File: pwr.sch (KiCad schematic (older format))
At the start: 54 parts, among them U1 FT601, U10 MIC94310, U11 PAM2305, U4 ECP5, U6 PAM2305, U7 NCP186, U8 MIC94310, U9 MIC94310, X2 CONN_01X08

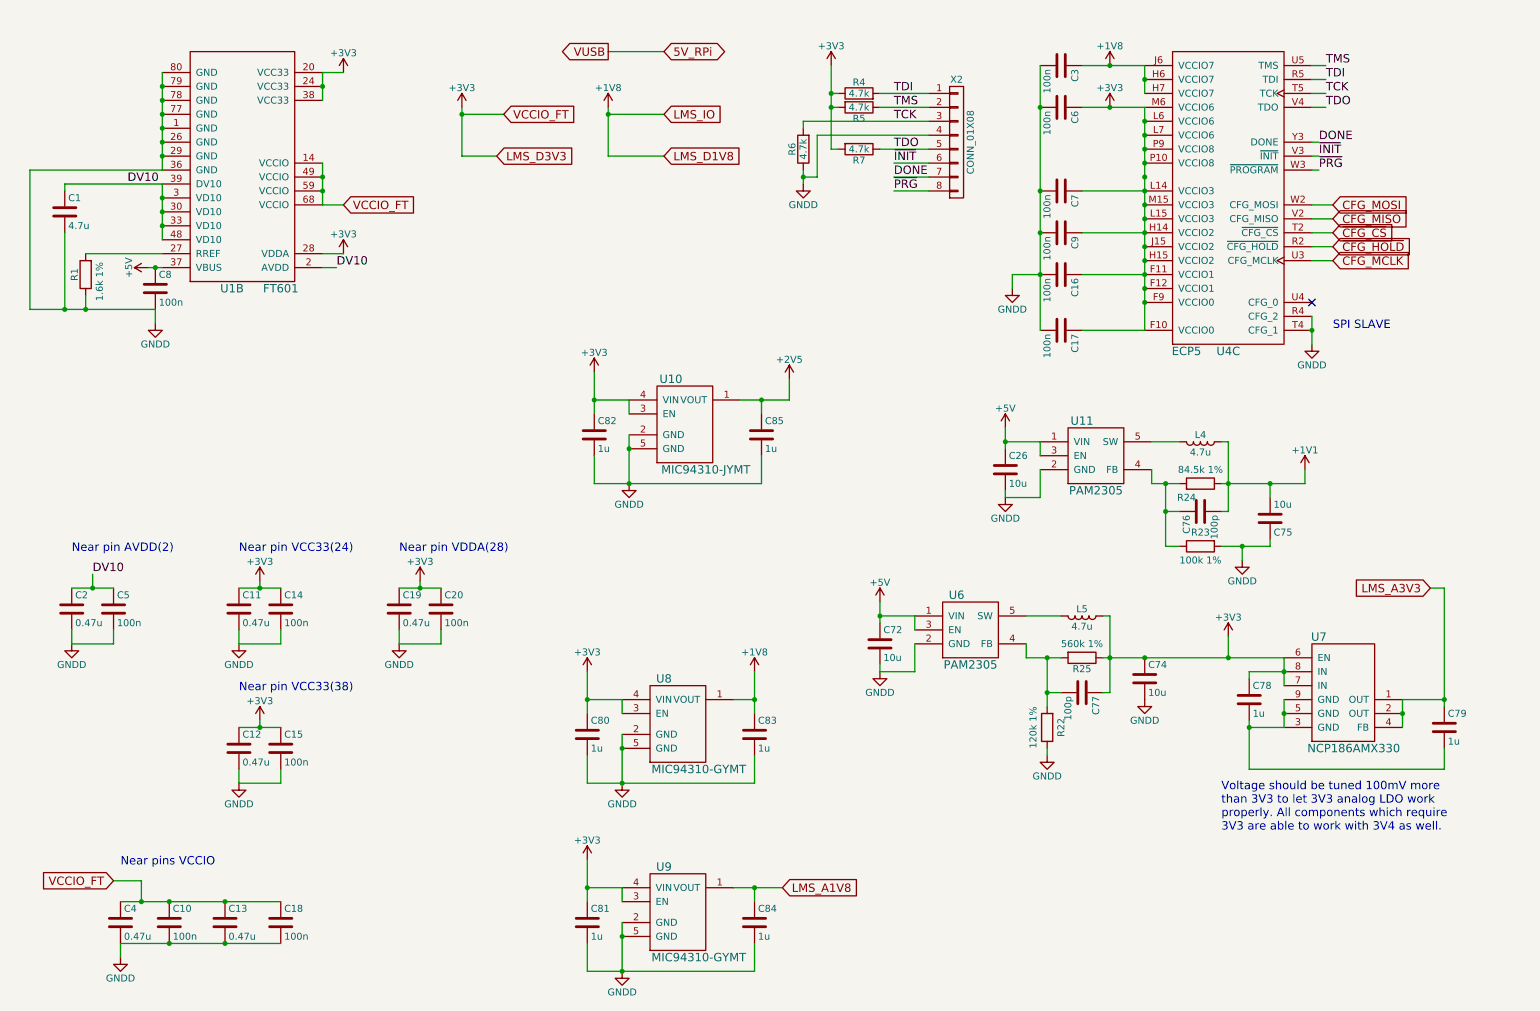
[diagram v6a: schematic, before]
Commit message: Start placing RF. Shield is ready. Fixed some net bugs.
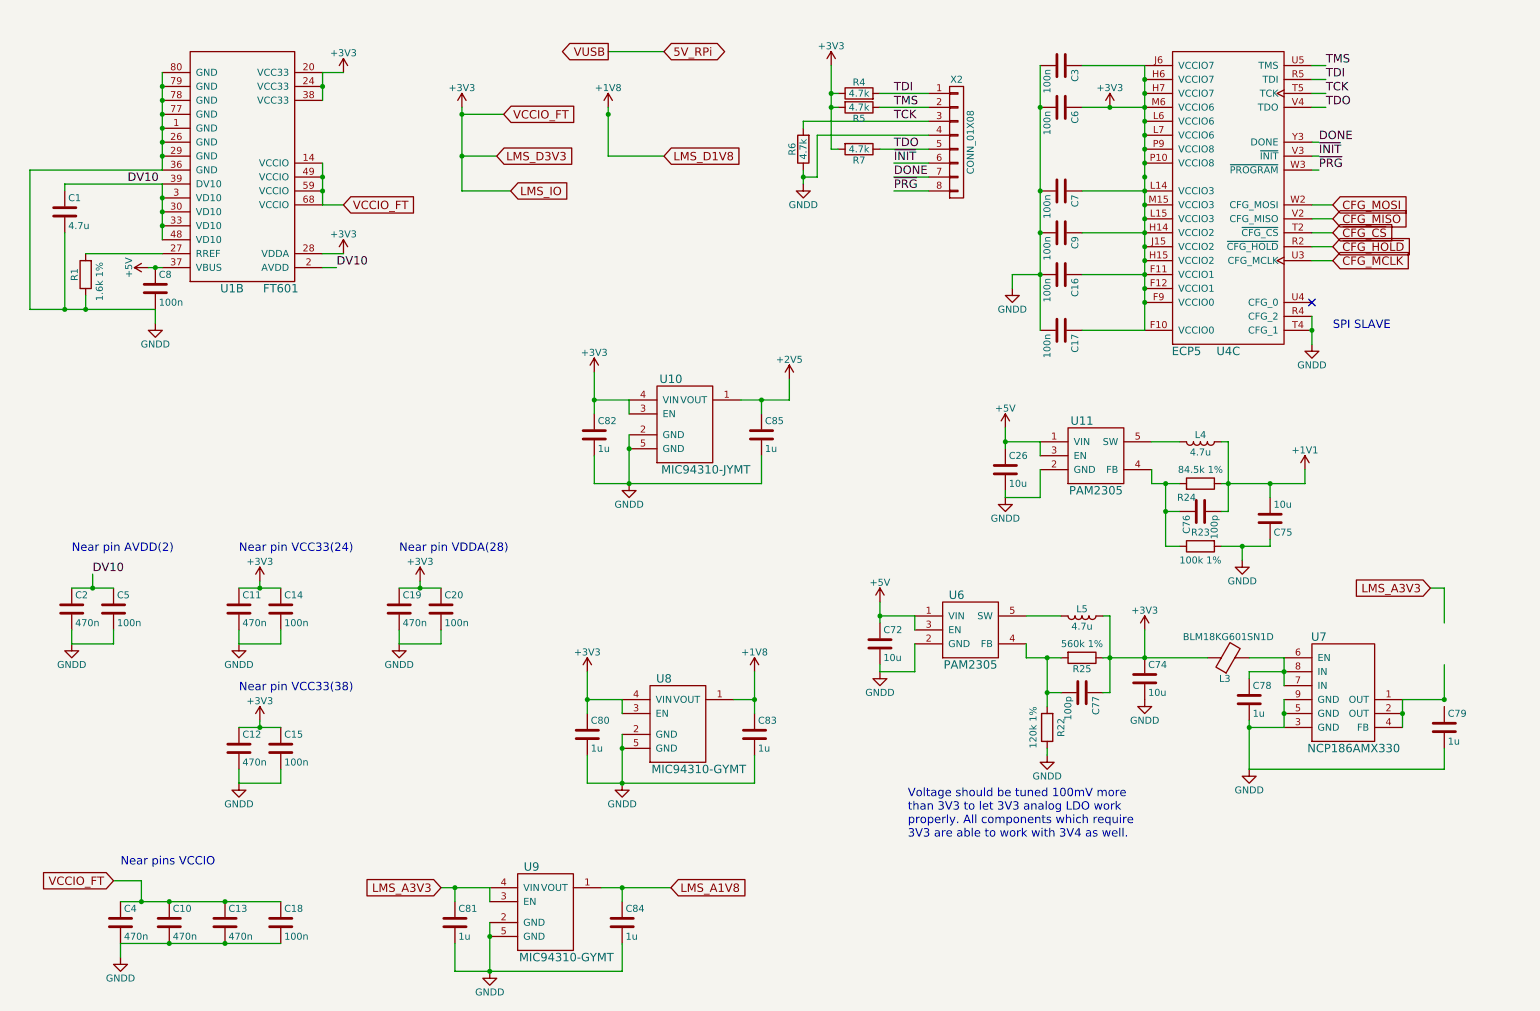
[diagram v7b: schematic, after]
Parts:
- added L3: BLM18KG601SN1D, Capacitors_SMD:C_0805, symbol Ferrite_Bead
- C10: value 100n -> 470n
- C11, C12, C13, C19, C2, C4: value 0.47u -> 470n
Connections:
- net +1V8: no longer C3.1, U4.H6 (VCCIO7), U4.H7 (VCCIO7), U4.J6 (VCCIO7)
- net +3V3: now also C3.1, U4.H6 (VCCIO7), U4.H7 (VCCIO7), U4.J6 (VCCIO7), L3.1; no longer C78.1, C81.1, U7.6 (EN), U7.7 (IN), U7.8 (IN), U9.3 (EN), U9.4 (VIN)
- net GNDD: now also C78.2, C79.2, U7.3 (GND), U7.5 (GND), U7.9 (GND)
- net LMS_A3V3: now also C81.1, U9.3 (EN), U9.4 (VIN); no longer C79.1, U7.1 (OUT), U7.2 (OUT), U7.4 (FB)
- new net: U7.1 (OUT), U7.2 (OUT), U7.4 (FB)
- new net: C78.1, L3.2, U7.6 (EN), U7.7 (IN), U7.8 (IN)
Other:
- moved on the sheet: C81, C84, U9

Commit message: Right before switching to full RPi
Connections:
- net +3V3: now also C78.1, U7.6 (EN), U7.7 (IN), U7.8 (IN); no longer L3.1
- net LMS_A3V3: now also L3.1
- net at U7.1 (OUT), U7.2 (OUT), U7.4 (FB): now also C79.1, L3.2
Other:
- moved on the sheet: L3
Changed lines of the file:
@@
 L Ferrite_Bead L3
 U 1 1 58C779A8
-P 9250 5200
-F 0 "L3" V 9100 5225 50  0000 C CNN
-F 1 "BLM18KG601SN1D" V 9400 5200 50  0000 C CNN
-F 2 "Capacitors_SMD:C_0805" V 9180 5200 50  0001 C CNN
-F 3 "" H 9250 5200 50  0000 C CNN
-	1    9250 5200
-	0    -1   -1   0
+P 10800 5050
+F 0 "L3" V 10650 5075 50  0000 C CNN
+F 1 "BLM18KG601SN1D" V 10950 5050 50  0000 C CNN
+F 2 "Capacitors_SMD:C_0805" V 10730 5050 50  0001 C CNN
+F 3 "" H 10800 5050 50  0000 C CNN
+	1    10800 5050
+	1    0    0    -1
 $EndComp
-Wire Wire Line
-	10800 5500 10800 5250
-Wire Wire Line
-	10800 4950 10800 4700
 Text GLabel 3600 6850 0    60   Input ~ 0
 LMS_A3V3
@@
 $EndComp
 Wire Wire Line
-	9400 5200 9650 5200
-Wire Wire Line
-	8350 5200 9100 5200
+	8350 5200 9650 5200
 Wire Wire Line
 	8650 5000 8650 5200
+Wire Wire Line
+	10800 5200 10800 5550
+Wire Wire Line
+	10800 4700 10800 4900
 $EndSCHEMATC
